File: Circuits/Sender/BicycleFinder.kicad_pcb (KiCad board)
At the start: 2 copper layers, 64.1 x 40.1 mm, 11 parts, among them CN1 WRITER, SW1 SW_PUSH, U1 LITE_LITE, U2 HN2S01FU

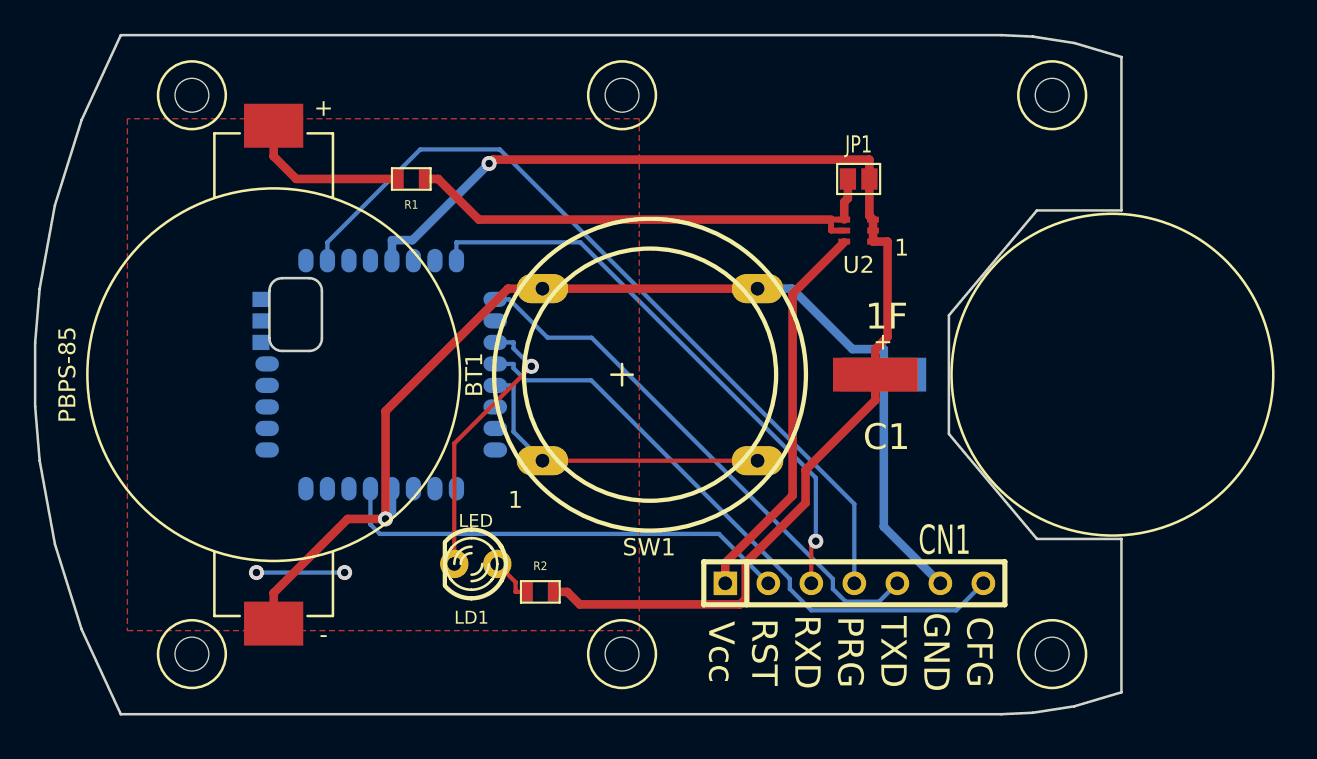
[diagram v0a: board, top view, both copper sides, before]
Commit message: Replaced EDLC.
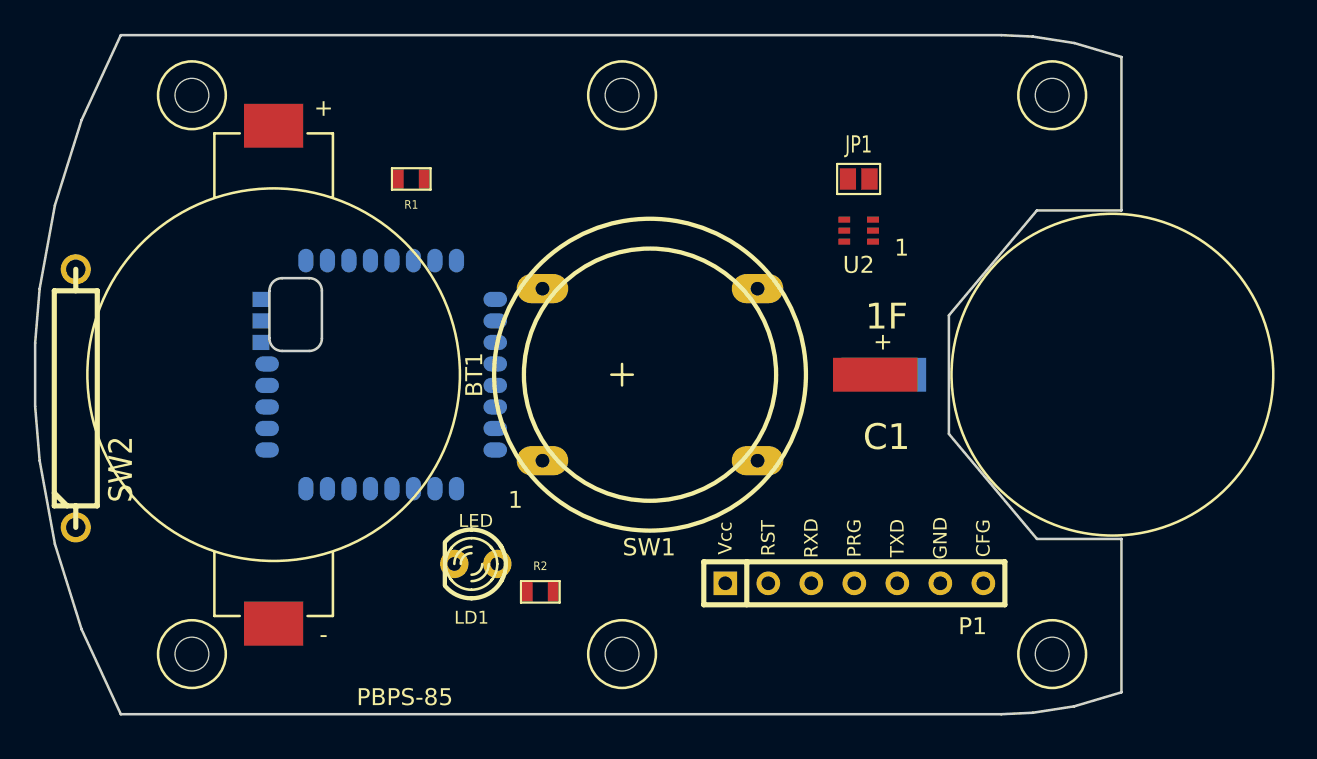
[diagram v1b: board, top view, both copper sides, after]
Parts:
- removed CN1: WRITER, SIL-7
- added P1: WRITER-VCC, WRITE-7P, F.Cu at (62.2, 46.2)
- added SW2: REED SW, R6, F.Cu at (16.3, 35.3)
- U1: value LITE_LITE -> TWE_LITE_SMD
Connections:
- net /DI1 renamed N-0000017
- net /DO4 renamed N-000003
- LD1 pad 1: /LED -> N-000002
- R2 pad 1: /LED -> /Vcc
- R2 pad 2: /Vcc -> N-000002
- U1 pad 12: /M1 -> N-0000013
- U1 pad 18: (no net) -> N-0000016
- U1 pad 2: /PRG -> N-0000014
- U1 pad 21: /RST -> N-0000012
- U1 pad 28: (no net) -> GND
- U1 pad 30: (no net) -> GND
- U1 pad 31: (no net) -> GND
- U1 pad 32: (no net) -> GND
- U1 pad 8: /RX -> N-0000019
- U1 pad 9: /TX -> N-000005
- U2 pad 6: /DC3V -> N-000001
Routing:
- net /Vcc: track 73.5 -> 0.00 mm, vias 1 -> 0
- net GND: track 67.6 -> 0.00 mm, vias 1 -> 0
- net /PRG: track 47.8 -> 0.00 mm
- net /M1: track 36.0 -> 0.00 mm
- net /RX: track 34.4 -> 0.00 mm, vias 1 -> 0
- net /TX: track 31.9 -> 0.00 mm
- net /CHG: track 29.7 -> 0.00 mm
- net /RST: track 27.0 -> 0.00 mm
- net /DC3V: track 23.1 -> 0.00 mm
- net N-0000017: track 18.9 -> 0.00 mm
- net N-000003: track 16.5 -> 0.00 mm, vias 1 -> 0
- net /3V: track 9.73 -> 0.00 mm
- net (no net): track 5.21 -> 0.00 mm, vias 2 -> 0
- net /LED: track 2.80 -> 0.00 mm
- removed copper zone on F.Cu, net (none)
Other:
- board text removed: "CFG"
- board text removed: "GND"
- board text removed: "PRG"
- board text removed: "RST"
- board text removed: "RXD"
- board text removed: "TXD"
- board text removed: "Vcc"

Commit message: Reviewing connections.
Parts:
- SW2: footprint R6 -> REEDSW
- moved LD1 21.2 mm to (21.6, 34.3), turned to 270 degrees
- moved R1 12.2 mm to (48.3, 22.9)
- moved BT1 6.99 mm to (34.3, 36.8), turned to 300 degrees
- moved SW1 6.36 mm to (56.5, 34.5)
- moved JP1 5.39 mm to (57.1, 21.6), turned to 0 degrees
- moved U2 4.72 mm to (59.7, 21.6), turned to 270 degrees
- moved R2 2.83 mm to (46.5, 47.2)
- moved U1 2.82 mm to (37.1, 34.3)
- moved SW2 1.42 mm to (17.5, 34.7)
- moved PBPS-85 0.77 mm to (49.0, 34.5)
- moved C1 0.71 mm to (78.0, 34.4), turned to 135 degrees
- moved P1 0.71 mm to (62.7, 46.7)
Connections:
- net N-0000016 renamed /STOP
- net N-0000017 renamed /WUP
- P1 pad 1: N-000001 -> N-0000013
- P1 pad 2: N-0000012 -> N-000005
- P1 pad 3: N-000005 -> N-0000012
- P1 pad 4: N-0000014 -> N-0000018
- P1 pad 5: N-0000019 -> GND
- P1 pad 6: GND -> N-0000014
- U1 pad 12: N-0000013 -> N-0000014
- U1 pad 2: N-0000014 -> N-0000012
- U1 pad 21: N-0000012 -> N-0000013
- U1 pad 8: N-0000019 -> N-0000018
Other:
- outline, holes or cut-outs redrawn

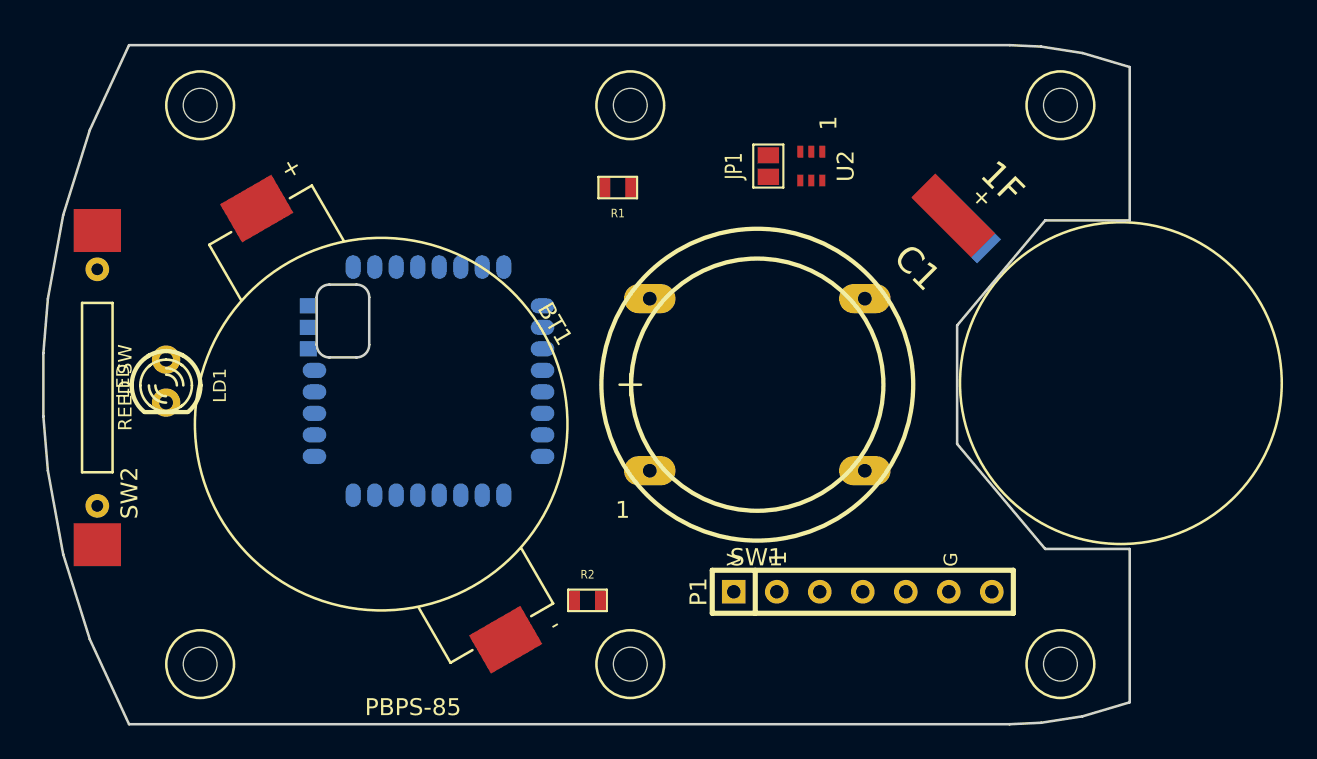
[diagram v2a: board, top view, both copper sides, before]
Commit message: Updated connections.
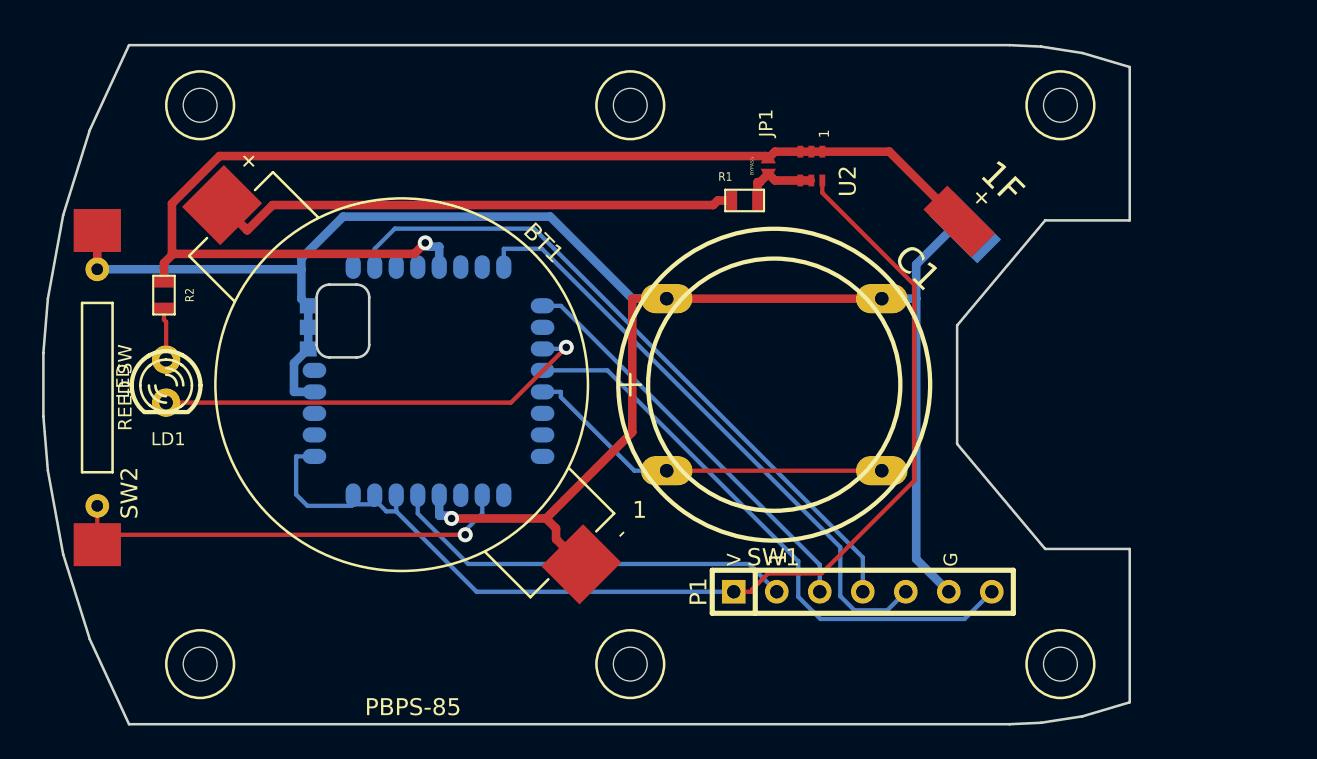
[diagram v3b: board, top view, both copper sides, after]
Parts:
- BT1: value 3V -> CR2032
- JP1: footprint GS2 -> JUMPER
- U1: footprint TWE-001L-SMD -> TWE-001L-NC7
- moved R2 30.8 mm to (21.5, 29.2), turned to 270 degrees
- moved R1 7.53 mm to (55.8, 23.6)
- moved BT1 2.63 mm to (35.5, 34.5), turned to 315 degrees
- moved SW1 1.00 mm to (57.5, 34.5)
- turned JP1 to 270 degrees
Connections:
- net N-0000012 renamed /PRG
- net N-0000013 renamed /RST
- net N-0000014 renamed /CFG
- net N-0000018 renamed /TXD
- net N-000002 renamed /LED
- net N-000003 renamed /DO4
- net N-000005 renamed /RXD
- P1 pad 0: N-000001 -> /ExVcc
- U1 pad 22: (no net) -> /ExVcc
- U1 pad 23: (no net) -> /ExVcc
- U1 pad 24: (no net) -> /ExVcc
- U1 pad 25: (no net) -> /ExVcc
- U2 pad 6: N-000001 -> /ExVcc
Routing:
- net GND: track 0.00 -> 115.3 mm, vias 0 -> 1
- net /Vcc: track 0.00 -> 71.3 mm, vias 0 -> 1
- net /ExVcc: track 0.00 -> 67.2 mm
- net /PRG: track 0.00 -> 40.5 mm
- net /TXD: track 0.00 -> 35.8 mm
- net /CFG: track 0.00 -> 34.5 mm
- net /3V: track 0.00 -> 31.4 mm
- net /STOP: track 0.00 -> 27.0 mm, vias 0 -> 1
- net /DO4: track 0.00 -> 26.4 mm, vias 0 -> 1
- net /RXD: track 0.00 -> 24.3 mm
- net /RST: track 0.00 -> 24.2 mm
- net /WUP: track 0.00 -> 22.1 mm
- net /CHG: track 0.00 -> 4.62 mm
- net /LED: track 0.00 -> 3.10 mm

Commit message: Added reset monitor.
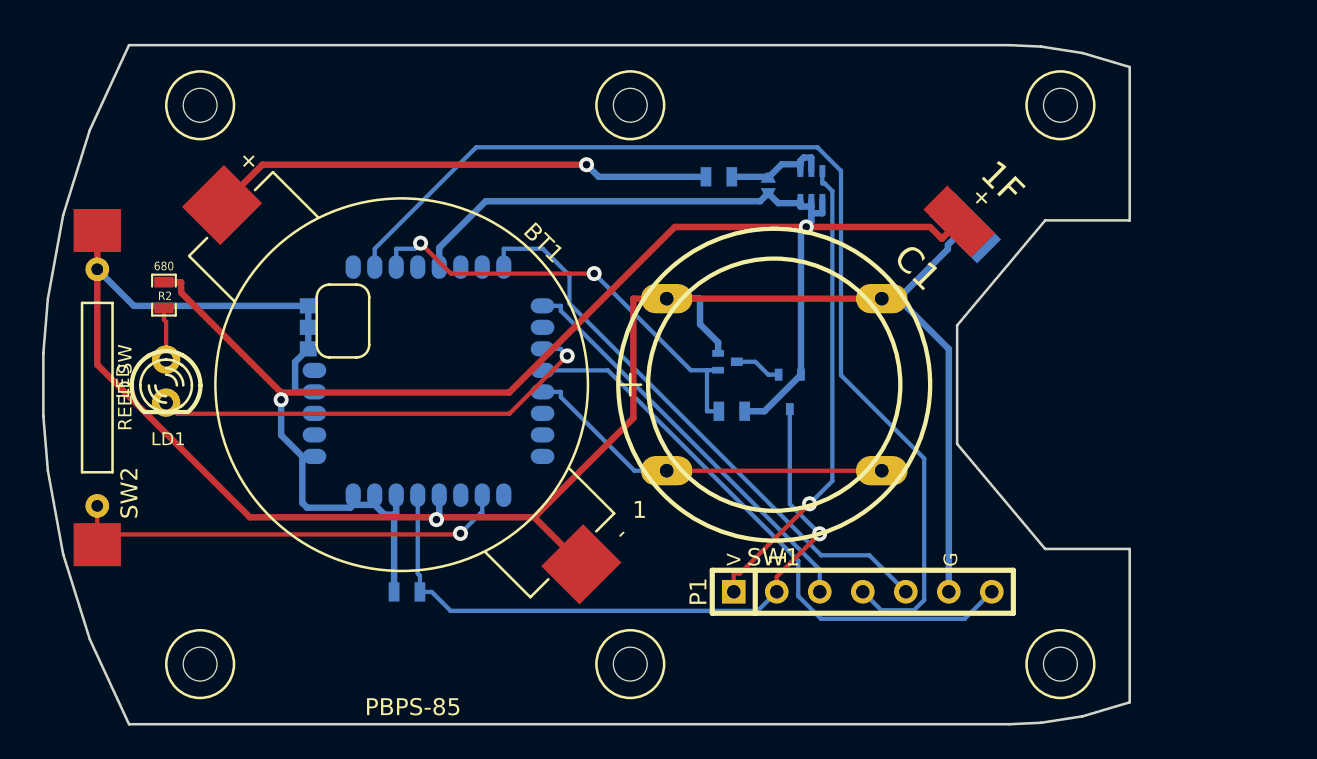
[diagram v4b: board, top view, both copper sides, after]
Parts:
- added Q1: MOS_N, EMT3, B.Cu at (54.7, 33.1)
- added R3: 10M, SM0603_Resistor, B.Cu at (55.0, 36.1)
- added R4: 10M, SM0603_Resistor, B.Cu at (35.8, 46.7)
- added U3: TCM809RVNB, sc70, B.Cu at (58.4, 34.9)
- JP1, U2: moved to B.Cu
- R1: footprint SM0603 -> SM0603_Resistor; moved to B.Cu
- R2: footprint SM0603 -> SM0603_Resistor
- U1: footprint TWE-001L-NC7 -> TWE-001L-SMD-noNTH
- moved R1 2.07 mm to (54.2, 22.2)
- moved JP1 1.14 mm to (57.1, 22.7), turned to 90 degrees
- moved U2 1.14 mm to (59.7, 22.7), turned to 90 degrees
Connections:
- U1 pad 22: /ExVcc -> /Vcc
- U1 pad 23: /ExVcc -> /Vcc
- U1 pad 24: /ExVcc -> /Vcc
- U1 pad 25: /ExVcc -> /Vcc
- U1 pad 3: (no net) -> /DO1
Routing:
- net /Vcc: track 71.3 -> 116.7 mm, vias 1 -> 2
- net /ExVcc: track 67.2 -> 27.8 mm, vias 0 -> 1
- net /DO1: track 0.00 -> 26.5 mm, vias 0 -> 2
- net /PRG: track 40.5 -> 63.4 mm
- net /RST: track 24.2 -> 40.3 mm, vias 0 -> 1
- net GND: track 115.3 -> 123.9 mm
- net /QGND: track 0.00 -> 2.79 mm
- net /CHG: track 4.62 -> 6.52 mm
- net /TXD: track 35.8 -> 34.2 mm
- net /3V: track 31.4 -> 29.9 mm, vias 0 -> 1
- net /DO4: track 26.4 -> 27.0 mm
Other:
- net class power: trace_width 0.508 -> 0.381
